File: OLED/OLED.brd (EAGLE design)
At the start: 58.4 x 25.4 mm, 15 parts

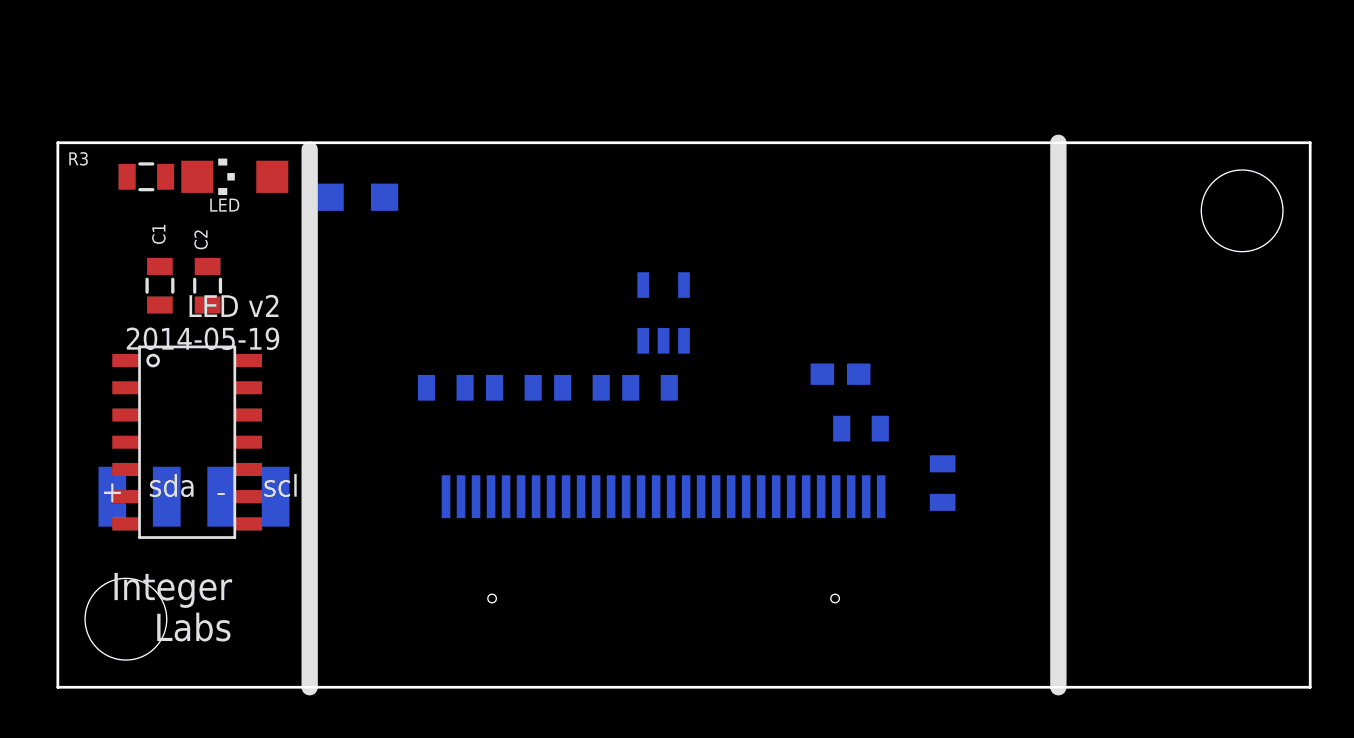
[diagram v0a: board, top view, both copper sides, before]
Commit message: Checking in current version of OLED board
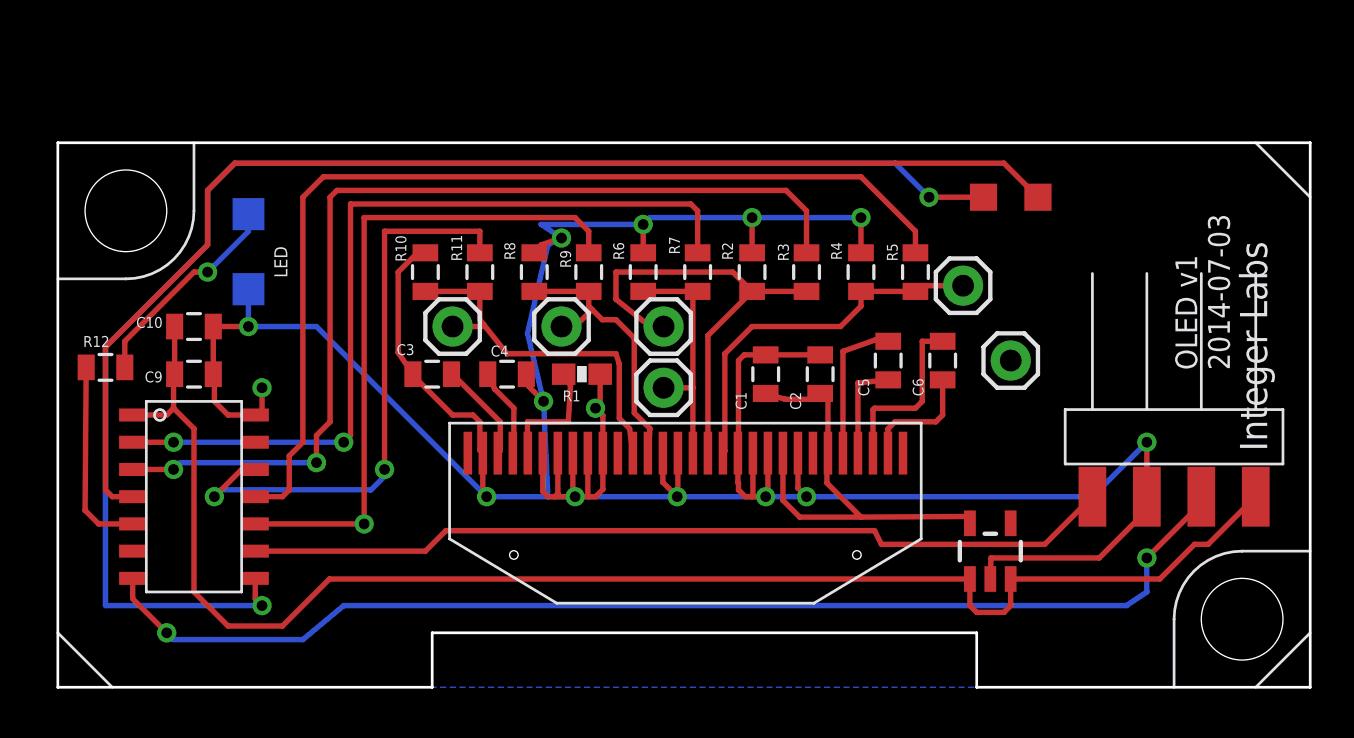
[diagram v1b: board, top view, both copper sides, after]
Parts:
- removed C7, C8: (no value), SparkFun-Capacitors:0805
- added C10: 10uF, SparkFun-Capacitors:0805
- added C9: 0.1uF, SparkFun-Capacitors:0805
- added JP1, JP2, JP3, JP4, JP5, JP6: M01PTH, SparkFun-Connectors:1X01
- added R10, R2, R4, R6, R8: 1k, SparkFun-Resistors:0805
- added R11, R5, R7, R9: 2k, SparkFun-Resistors:0805
- added R12: 680, SparkFun-Passives:0805
- C3, C4: value (none) -> 2.2uF
- C5, C6: value (none) -> 1uF
- R3: value 175 -> 2k; device SparkFun-Passives:0805 -> SparkFun-Resistors:0805
- U$4: value FOOTPRINTDOUBLE -> FOOTPRINTDOUBLE-NODIM; device IntegerLabs:FOOTPRINT-DOUBLE -> IntegerLabs:FOOTPRINT-DOUBLE-NODIMENSION
- moved U$4 58.4 mm to (58.4, 0.00), flipped to the bottom
- moved R3 31.1 mm to (34.9, 19.4), turned to 90 degrees
- moved C2 28.9 mm to (35.6, 14.6), turned to 270 degrees
- moved C1 28.6 mm to (33.0, 14.6), turned to 270 degrees
- moved C3 24.3 mm to (17.5, 14.6), flipped to the top, turned to 180 degrees
- moved C6 23.2 mm to (41.3, 15.2), flipped to the top, turned to 270 degrees
- moved U$2 18.9 mm to (43.5, 6.35), flipped to the top
- moved C5 17.5 mm to (38.7, 15.2), flipped to the top, turned to 270 degrees
- moved C4 16.7 mm to (21.0, 14.6), flipped to the top, turned to 0 degrees
- moved R1 12.1 mm to (24.4, 14.6), flipped to the top, turned to 180 degrees
- moved LED 3.55 mm to (8.89, 20.3), flipped to the bottom, turned to 180 degrees
- moved U$3 2.56 mm to (6.67, 12.7)
- moved U$1 2.27 mm to (29.3, 10.9), flipped to the top
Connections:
- net SCL/SCK renamed BUS_CLK
- net SDA/MOSI renamed BUS_DATA
- removed net DATA: U$3.11
- removed net MISO: U$3.8
- new net CS: R5.2, U$3.11
- new net D/C: R7.2, U$3.2
- new net MOSI: R11.2, U$3.12
- new net N$13: JP3.1, R6.2, R7.1, U$1.P$15
- new net N$14: JP2.1, R4.2, R5.1, U$1.P$13
- new net N$15: JP1.1, R2.2, R3.1, U$1.P$14
- new net N$7: JP5.1, R10.2, R11.1, U$1.P$19
- new net N$8: JP4.1, R8.2, R9.1, U$1.P$18
- new net PGM_MISO: U$3.8, U$4.MISO
- new net PGM_RESET: U$3.4, U$4.RESET
- new net SCK: R9.2, U$3.10
- net +3.3V: now also C1.2, C2.2, U$1.P$6; no longer C8.2
- net +5V: now also C10.2, C9.2, U$2.3; no longer C1.2, C2.2, C7.2, U$1.P$6
- net GND: now also C10.1, C9.1, JP6.1, R10.1, R2.1, R4.1, R6.1, R8.1, U$1.P$10, U$1.P$11, U$1.P$12, U$1.P$16, U$1.P$17, U$1.P$21, U$1.P$22, U$1.P$23, U$1.P$24, U$1.P$25; no longer C7.1, C8.1
- net LED: now also R12.2, U$3.5; no longer R3.2, U$3.12
- net N$5: now also R12.1; no longer R3.1
- net RESET: now also R3.2, U$3.3; no longer U$3.4
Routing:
- net GND: track 0.00 -> 158.8 mm, vias 0 -> 14
- net +5V: track 0.00 -> 70.3 mm
- net PGM_MISO: track 0.00 -> 67.4 mm, vias 0 -> 2
- net PGM_RESET: track 0.00 -> 57.3 mm
- net BUS_DATA: track 0.00 -> 55.3 mm, vias 0 -> 2
- net CS: track 0.00 -> 46.7 mm
- net RESET: track 0.00 -> 46.1 mm, vias 0 -> 2
- net BUS_CLK: track 0.00 -> 40.8 mm
- net D/C: track 0.00 -> 39.4 mm, vias 0 -> 2
- net SCK: track 0.00 -> 31.1 mm, vias 0 -> 1
- net MOSI: track 0.00 -> 27.6 mm, vias 0 -> 2
- net N$15: track 0.00 -> 21.6 mm
- net +3.3V: track 0.00 -> 21.1 mm
- net N$14: track 0.00 -> 17.5 mm
- net N$7: track 0.00 -> 17.3 mm
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- added copper zone on layer 16, net GND
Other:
- outline, holes or cut-outs redrawn
- board text added: "OLED v1 2014-07-03"
- board text removed: "+"
- board text removed: "-"
- board text removed: "LED v2 2014-05-19"
- board text removed: "scl"
- board text removed: "sda"

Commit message: New OLED design for v2 footprint.
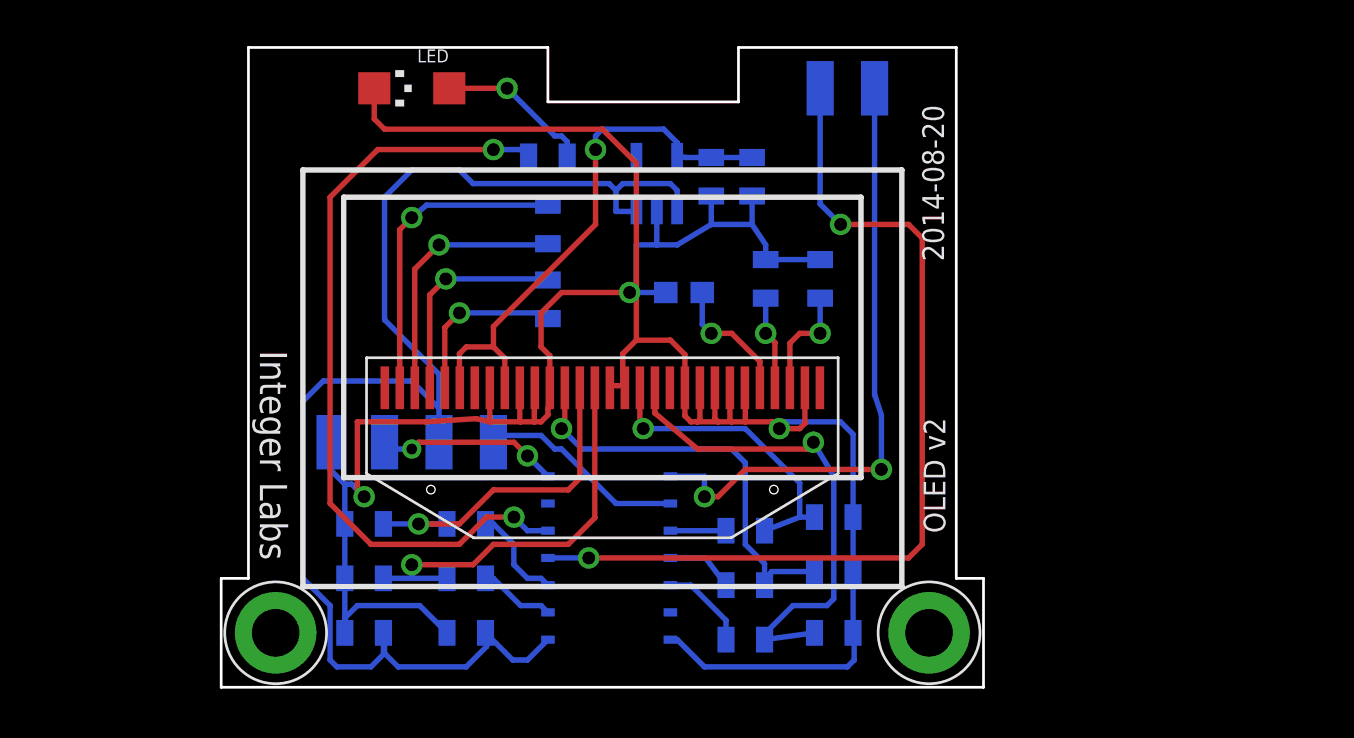
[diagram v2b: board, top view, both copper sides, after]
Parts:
- removed JP1, JP2, JP3, JP4, JP5, JP6: M01PTH, SparkFun-Connectors:1X01
- removed U$4: FOOTPRINTDOUBLE-NODIM, IntegerLabs:FOOTPRINT-DOUBLE-NODIMENSION
- added U$5: FOOTPRINTFOOTPRINT-2, IntegerLabs:FOOTPRINT2
- R10, R2, R4, R6, R8: value 1k -> 2k
- R11, R3, R5, R7, R9: value 2k -> 1k
- U$1: value OLED -> OLEDREVERSE; device IntegerLabs:FPC-30 -> IntegerLabs:FPC-30-REVERSE
- moved R10 25.4 mm to (36.2, 2.54), flipped to the bottom, turned to 0 degrees
- moved U$2 23.2 mm to (27.9, 23.5), flipped to the bottom
- moved R12 22.9 mm to (22.9, 24.8), flipped to the bottom, turned to 0 degrees
- moved U$3 22.0 mm to (26.0, 2.22), flipped to the bottom, turned to 90 degrees
- moved R2 21.6 mm to (14.3, 7.62), flipped to the bottom, turned to 180 degrees
- moved R11 21.1 mm to (32.1, 2.22), flipped to the bottom, turned to 0 degrees
- moved R3 19.7 mm to (19.1, 7.62), flipped to the bottom, turned to 180 degrees
- moved C6 19.5 mm to (22.9, 21.6), flipped to the bottom, turned to 90 degrees
- moved R6 19.3 mm to (14.3, 5.08), flipped to the bottom, turned to 180 degrees
- moved C3 18.6 mm to (35.6, 19.1), flipped to the bottom, turned to 90 degrees
- moved R8 18.1 mm to (36.2, 7.94), flipped to the bottom, turned to 0 degrees
- moved R7 17.9 mm to (19.1, 5.08), flipped to the bottom, turned to 180 degrees
- moved C9 17.5 mm to (19.1, 2.54), flipped to the bottom
- moved R5 16.6 mm to (32.1, 4.76), flipped to the bottom, turned to 0 degrees
- moved C10 16.3 mm to (14.3, 2.54), flipped to the bottom
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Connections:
- net +3.3V: now also U$1.6, U$1.9; no longer U$1.P$6, U$1.P$9
- net +5V: now also U$5.VCC; no longer U$4.P$1
- net BUS_CLK: now also U$5.SCL; no longer U$4.P$4
- net BUS_DATA: now also U$5.SDA; no longer U$4.P$2
- net GND: now also U$1.10, U$1.11, U$1.12, U$1.16, U$1.17, U$1.21, U$1.22, U$1.23, U$1.24, U$1.25, U$1.29, U$1.8, U$5.GND; no longer JP6.1, U$1.P$10, U$1.P$11, U$1.P$12, U$1.P$16, U$1.P$17, U$1.P$21, U$1.P$22, U$1.P$23, U$1.P$24, U$1.P$25, U$1.P$29, U$1.P$8, U$4.P$3
- net N$10: now also U$1.2; no longer U$1.P$2
- net N$11: now also U$1.5; no longer U$1.P$5
- net N$12: now also U$1.3; no longer U$1.P$3
- net N$13: now also U$1.15; no longer JP3.1, U$1.P$15
- net N$14: now also U$1.13; no longer JP2.1, U$1.P$13
- net N$15: now also U$1.14; no longer JP1.1, U$1.P$14
- net N$2: now also U$1.26; no longer U$1.P$26
- net N$4: now also U$1.28; no longer U$1.P$28
- net N$6: now also U$1.27; no longer U$1.P$27
- net N$7: now also U$1.19; no longer JP5.1, U$1.P$19
- net N$8: now also U$1.18; no longer JP4.1, U$1.P$18
- net N$9: now also U$1.4; no longer U$1.P$4
- net PGM_MISO: now also U$5.MISO; no longer U$4.MISO
- net PGM_RESET: now also U$5.RESET; no longer U$4.RESET
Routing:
- net BUS_DATA: track 55.3 -> 8.73 mm
- net CS: track 46.7 -> 3.23 mm
- net RESET: track 46.1 -> 4.65 mm, vias 2 -> 0
- net PGM_MISO: track 67.4 -> 29.2 mm
- net D/C: track 39.4 -> 3.57 mm, vias 2 -> 0
- net BUS_CLK: track 40.8 -> 10.2 mm
- net SCK: track 31.1 -> 2.59 mm, vias 1 -> 0
- net GND: track 158.8 -> 131.1 mm, vias 14 -> 3
- net LED: track 9.15 -> 36.3 mm, vias 0 -> 2
- net MOSI: track 27.6 -> 4.17 mm, vias 2 -> 0
- net PGM_RESET: track 57.3 -> 42.8 mm, vias 0 -> 2
- net N$10: track 5.59 -> 14.7 mm, vias 0 -> 1
- net N$13: track 11.5 -> 19.1 mm, vias 0 -> 1
- net N$7: track 17.3 -> 23.4 mm, vias 0 -> 1
- net N$9: track 4.70 -> 10.2 mm, vias 0 -> 1
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- removed copper zone on layer 16, net GND
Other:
- board size 58.4 x 25.4 mm -> 35.6 x 29.8 mm
- board text added: "2014-08-20"
- board text added: "OLED v2"
- board text removed: "OLED v1 2014-07-03"

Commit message: minor revisions
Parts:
- removed C1, C9: 0.1uF, SparkFun-Capacitors:0805
- removed R10, R4, R6, R8: 2k, SparkFun-Resistors:0805
- removed R11, R3, R5, R7, R9: 1k, SparkFun-Resistors:0805
- added Q1, Q2: MOSFET-NCHANNELBSS138, SparkFun-DiscreteSemi:SOT23
- added R13, R14: 2k, SparkFun-Passives:0805
- added U$4: FOOTPRINTFOOTPRINT-2, IntegerLabs:FOOTPRINT2
- added U$6, U$7: TACT-SWITCHKMR2, IntegerLabs:TACT-SWITCH-SMALL
- C10, C2: value 10uF -> .47uF
- R2: value 2k -> 1; device SparkFun-Resistors:0805 -> SparkFun-Passives:0805
- U$5: value FOOTPRINTFOOTPRINT-2 -> TACT-SWITCHKMR2; device IntegerLabs:FOOTPRINT2 -> IntegerLabs:TACT-SWITCH-SMALL
- moved R12 14.0 mm to (9.21, 27.9), turned to 90 degrees
- moved C10 9.09 mm to (6.03, 6.35), turned to 0 degrees
- moved C5 8.89 mm to (14.0, 18.1)
- moved R2 8.28 mm to (6.03, 8.26)
- moved U$2 7.73 mm to (20.3, 22.2)
- moved C4 7.62 mm to (25.4, 19.1)
- moved C3 7.62 mm to (27.9, 19.1)
- moved R1 7.62 mm to (21.6, 18.4)
- moved C6 7.62 mm to (15.2, 21.6)
- moved C2 7.62 mm to (24.8, 23.8)
- moved U$1 7.62 mm to (17.8, 11.4)
- moved U$3 7.55 mm to (19.1, 5.08)
- moved U$5 2.54 mm to (7.62, 2.54)
- moved LED 1.27 mm to (17.8, 27.9)
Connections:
- removed net BUS_CLK: U$3.9, U$5.SCL
- removed net BUS_DATA: U$3.7, U$5.SDA
- removed net CS: R5.2, U$3.11
- removed net D/C: R7.2, U$3.2
- removed net LED: R12.2, U$3.5
- removed net MOSI: R11.2, U$3.12
- removed net N$13: R6.2, R7.1, U$1.15
- removed net N$14: R4.2, R5.1, U$1.13
- removed net N$15: R2.2, R3.1, U$1.14
- removed net N$5: LED.A, R12.1
- removed net N$8: R8.2, R9.1, U$1.18
- removed net PGM_MISO: U$3.8, U$5.MISO
- removed net PGM_RESET: U$3.4, U$5.RESET
- removed net SCK: R9.2, U$3.10
- new net BUTTON1: U$3.2, U$5.P1
- new net BUTTON2: U$3.3, U$6.P1
- new net BUTTON3: U$3.13, U$7.P1
- new net DISPLAY_CS: U$1.13, U$3.11
- new net DISPLAY_D/C: U$1.15, U$3.5
- new net DISPLAY_MOSI: U$1.19, U$3.12
- new net DISPLAY_RESET: U$1.14, U$3.6
- new net DISPLAY_SCK: U$1.18, U$3.10
- new net MISO/LED: LED.A, U$3.8, U$4.PROG3
- new net N$3: R2.2, U$4.BUS2
- new net SCL3.3/SCK: Q2.2, R14.1, U$3.9, U$4.PROG2
- new net SCL5: Q2.3, U$4.BUS3
- new net SDA3.3/MOSI: Q1.2, R13.1, U$3.7, U$4.PROG4
- new net SDA5: Q1.3, U$4.BUS1
- net +3.3V: now also Q1.1, Q2.1, R13.2, R14.2, U$3.1, U$4.PROG0; no longer C1.2
- net +5V: now also R2.1; no longer C9.2, U$3.1, U$5.VCC
- net GND: now also R12.1, U$4.BUS0, U$5.N1, U$5.N2, U$6.N1, U$6.N2, U$7.N1; no longer C1.1, C9.1, LED.C, R10.1, R2.1, R4.1, R6.1, R8.1, U$5.GND
- net N$7: now also LED.C, R12.2; no longer R10.2, R11.1, U$1.19
- net RESET: now also U$3.4, U$4.PROG1; no longer R3.2, U$3.3
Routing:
- net SDA3.3/MOSI: track 0.00 -> 60.9 mm, vias 0 -> 2
- net SCL3.3/SCK: track 0.00 -> 44.7 mm, vias 0 -> 3
- net PGM_RESET: track 42.8 -> 0.00 mm, vias 2 -> 0
- net MISO/LED: track 0.00 -> 42.1 mm, vias 0 -> 2
- net RESET: track 4.65 -> 46.6 mm, vias 0 -> 2
- net LED: track 36.3 -> 0.00 mm, vias 2 -> 0
- net +3.3V: track 25.6 -> 59.1 mm, vias 1 -> 2
- net PGM_MISO: track 29.2 -> 0.00 mm, vias 2 -> 0
- net SCL5: track 0.00 -> 26.5 mm, vias 0 -> 2
- net N$14: track 20.0 -> 0.00 mm, vias 1 -> 0
- net +5V: track 64.9 -> 44.9 mm
- net N$13: track 19.1 -> 0.00 mm, vias 1 -> 0
- net BUTTON1: track 0.00 -> 17.4 mm, vias 0 -> 1
- net DISPLAY_CS: track 0.00 -> 16.4 mm, vias 0 -> 1
- net N$15: track 16.3 -> 0.00 mm, vias 1 -> 0
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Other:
- board size 35.6 x 29.8 mm -> 36.8 x 29.8 mm
- board text added: "Modulo"
- board text added: "OLED Display"
- board text added: "v3 2014-11-24"
- board text removed: "2014-08-20"
- board text removed: "OLED v2"

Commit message: Checkpointing PCB designs
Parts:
- LED: device led:CHIPLED_1206 -> adafruit:CHIP-LED0805
- U$5, U$6, U$7: value TACT-SWITCHKMR2 -> TACT-SWITCHBOURNS-7914J; device IntegerLabs:TACT-SWITCH-SMALL -> IntegerLabs:BOURNS-7914J
- moved R12 4.24 mm to (13.3, 27.0), flipped to the top
- moved C5 3.19 mm to (17.1, 18.4)
- turned U$5 to 270 degrees
- turned U$6 to 270 degrees
- turned U$7 to 270 degrees
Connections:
- net BUTTON1: now also U$5.POS$1; no longer U$5.P1
- net BUTTON2: now also U$6.POS$1; no longer U$6.P1
- net BUTTON3: now also U$7.POS$1; no longer U$7.P1
- net GND: now also U$5.NEG$1, U$5.NEG$2, U$6.NEG$1, U$6.NEG$2, U$7.NEG$1, U$7.NEG$2; no longer U$5.N1, U$5.N2, U$6.N1, U$6.N2, U$7.N1
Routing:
- net GND: track 136.1 -> 129.7 mm, vias 5 -> 3
- net BUTTON1: track 17.4 -> 13.5 mm
- net N$7: track 7.20 -> 3.52 mm, vias 1 -> 0
- net BUTTON3: track 10.5 -> 13.9 mm
- net N$9: track 8.89 -> 12.1 mm
- net N$11: track 6.69 -> 9.81 mm
- net SCL5: track 26.5 -> 25.6 mm
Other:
- board size 36.8 x 29.8 mm -> 36.3 x 29.8 mm
- board text removed: "Integer Labs"
- board text removed: "Modulo"
- board text removed: "OLED Display"
- board text removed: "v3 2014-11-24"
